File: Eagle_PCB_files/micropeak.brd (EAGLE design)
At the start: 100 x 80 mm, 15 parts, among them U1 ATTINY85-20MUR, U2 MS5611-01BA03

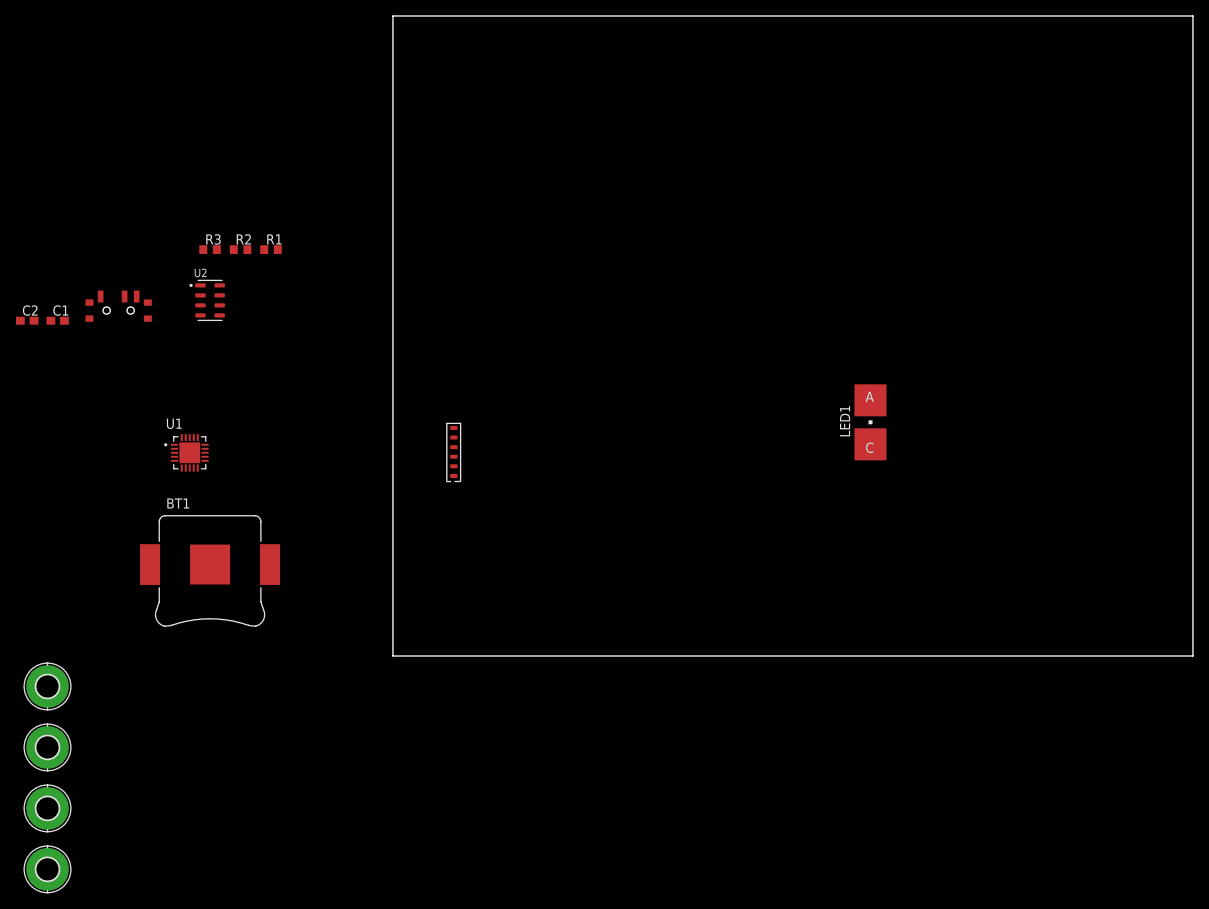
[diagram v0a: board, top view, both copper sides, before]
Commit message: made 18x14mm board outline
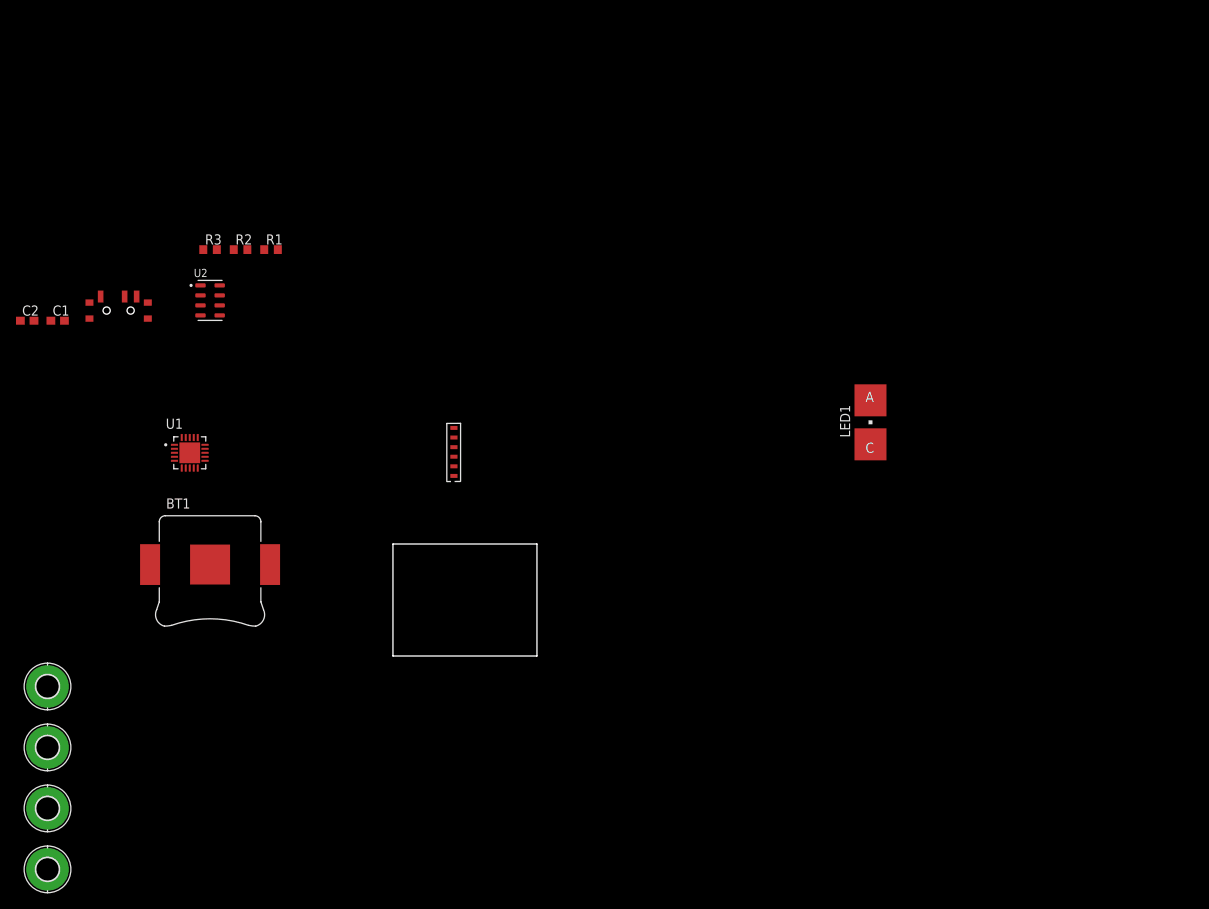
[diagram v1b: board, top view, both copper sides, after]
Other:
- board size 100 x 80 mm -> 18 x 14 mm
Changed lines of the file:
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@@
 <setting verticaltext="up"/>
 </settings>
-<grid distance="50" unitdist="mil" unit="mil" style="lines" multiple="1" display="no" altdistance="5" altunitdist="mil" altunit="mil"/>
+<grid distance="1" unitdist="mm" unit="mm" style="lines" multiple="1" display="no" altdistance="0.1" altunitdist="mm" altunit="mm"/>
 <layers>
 <layer number="1" name="Top" color="4" fill="1" visible="yes" active="yes"/>
@@
 <board>
 <plain>
-<wire x1="0" y1="0" x2="100" y2="0" width="0" layer="20"/>
-<wire x1="100" y1="0" x2="100" y2="80" width="0" layer="20"/>
-<wire x1="100" y1="80" x2="0" y2="80" width="0" layer="20"/>
-<wire x1="0" y1="80" x2="0" y2="0" width="0" layer="20"/>
+<wire x1="0" y1="0" x2="0" y2="14" width="0.1524" layer="20"/>
+<wire x1="0" y1="14" x2="18" y2="14" width="0.1524" layer="20"/>
+<wire x1="18" y1="14" x2="18" y2="0" width="0.1524" layer="20"/>
+<wire x1="18" y1="0" x2="0" y2="0" width="0.1524" layer="20"/>
 </plain>
 <attributes>

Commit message: prelim floorplanning started
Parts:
- moved H3 71.3 mm to (16.5, 12.3)
- moved H2 62.9 mm to (16.2, 1.55)
- moved LED1 56.0 mm to (9.79, 3.69), turned to 90 degrees
- moved R3 54.4 mm to (9.14, 6.80)
- moved U$1 53.4 mm to (9.09, 12.1), turned to 180 degrees
- moved H4 47.8 mm to (1.82, 12.4)
- moved H1 46.8 mm to (1.72, 1.77)
- moved U2 45.7 mm to (3.55, 7.14), turned to 90 degrees
- moved U1 43.4 mm to (14.3, 7.80)
- moved BT1 32.1 mm to (9.04, 7.73), flipped to the bottom
- moved U$2 21.8 mm to (11.9, 1.12), turned to 270 degrees

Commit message: have holes and outline positioned correctly - floorplanning done pretty much
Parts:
- removed H1, H2, H3, H4: MOUNT-PAD-ROUND2.8, holes:2,8-PAD
- removed LED1: (no value), led:P-LCC-2
- added U$3: LED, LED_LYT68B-T2V1-26-Z:LED_LYT68B-T2V1-26-Z
- added U$4, U$5, U$6, U$7: (no value), LED_LYT68B-T2V1-26-Z:2,8-PAD
- moved C2 62.7 mm to (6.28, 6.91)
- moved C1 53.0 mm to (3.09, 13.9)
- moved R3 21.5 mm to (17.1, 26.8)
- moved BT1 4.50 mm to (9.99, 12.1)
- moved U2 4.50 mm to (4.20, 11.6)
- moved U$1 4.33 mm to (9.59, 16.4)
- moved U$2 4.31 mm to (12.8, 5.32)
- moved U1 4.00 mm to (15.4, 11.7)
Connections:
- net +3V3: now also U$4.B2,8, U$5.B2,8, U$6.B2,8, U$7.B2,8; no longer H1.B2,8, H2.B2,8, H3.B2,8, H4.B2,8
- net GND: now also U$3.C; no longer LED1.C
- net N$4: now also U$3.A; no longer LED1.A

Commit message: routing done
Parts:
- removed C2: (no value), rcl:C0603
- removed R3: (no value), rcl:R0603
- added C3: (no value), rcl:C0402
- added R4: (no value), rcl:R0402
- C1: device rcl:C0603 -> rcl:C0402
- R1, R2: device rcl:R0603 -> rcl:R0402
- moved R2 48.5 mm to (11.1, 12.8)
- moved R1 42.0 mm to (5.70, 14.3), turned to 180 degrees
- moved C1 5.36 mm to (4.70, 8.80)
- moved U$3 0.35 mm to (9.70, 10.0)
- moved U1 0.33 mm to (15.1, 11.7)
- moved U$1 0.32 mm to (9.84, 16.6)
- moved BT1 0.21 mm to (10.0, 11.9)
- moved U$2 0.14 mm to (12.9, 5.42)
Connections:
- new net N$11: U$1.P$6
- new net N$12: U$1.P$7
- net +3V3: now also C3.1, R4.2; no longer C2.1, R2.2
- net GND: now also C3.2; no longer C2.2, U$1.P$6, U$1.P$7
- net MOSI: now also R1.1; no longer R3.1
- net N$2: now also R4.1; no longer R2.1
- net N$3: now also R2.2; no longer R1.1
- net N$4: now also R2.1; no longer R1.2
- net N$5: now also R1.2; no longer R3.2
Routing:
- net GND: track 0.00 -> 50.3 mm, vias 0 -> 2
- net MISO: track 0.00 -> 40.1 mm, vias 0 -> 2
- net SCK: track 0.00 -> 37.3 mm, vias 0 -> 2
- net MOSI: track 0.00 -> 33.6 mm, vias 0 -> 2
- net +3V3: track 0.00 -> 23.2 mm, vias 0 -> 1
- net CS_BARO: track 0.00 -> 19.2 mm, vias 0 -> 2
- net !RESET!: track 0.00 -> 13.1 mm
- net N$1: track 0.00 -> 5.87 mm, vias 0 -> 1
- net N$3: track 0.00 -> 3.28 mm
- net N$4: track 0.00 -> 3.07 mm
- net N$2: track 0.00 -> 2.28 mm
- net N$5: track 0.00 -> 1.72 mm
- added copper zone on layer 1, net +3V3
- added copper zone on layer 16, net +3V3
